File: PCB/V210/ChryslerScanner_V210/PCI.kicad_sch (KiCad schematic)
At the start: 15 parts, among them Q14 SI1555DL, U10 TS391C

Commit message: WIP
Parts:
- removed U10: TS391C, symbol ChryslerScanner:TS391C
- added U10: TS391RILT, Package_TO_SOT_SMD:SOT-23-5, symbol ChryslerScanner:TS391RILT
- C29, C30: footprint (none) -> Capacitor_SMD:C_0603_1608Metric
- D10: renamed from D18; value MSK4005 -> STPS0540Z; footprint (none) -> Britishideas:SOD-123; manf# (none) -> STPS0540Z
- D11: renamed from D19; value ESD585 -> ESD5B5; footprint (none) -> Diode_SMD:D_SOD-523; manf# (none) -> ESD5B5.0ST5G
- Q6: renamed from Q14; value SI1555DL -> BSD235CH6327XTSA1; footprint Package_TO_SOT_SMD:SOT-23-6 -> Package_TO_SOT_SMD:SOT-363_SC-70-6; manf# (none) -> BSD235CH6327XTSA1
- R36: renamed from R58; footprint (none) -> Resistor_SMD:R_0603_1608Metric
- R37: renamed from R59; footprint (none) -> Resistor_SMD:R_0603_1608Metric
- R38: renamed from R60; footprint (none) -> Resistor_SMD:R_0603_1608Metric
- R39: renamed from R61; footprint (none) -> Resistor_SMD:R_0603_1608Metric
- R40: renamed from R62; footprint (none) -> Resistor_SMD:R_0603_1608Metric
- R41: renamed from R63; footprint (none) -> Resistor_SMD:R_0603_1608Metric
- R42: renamed from R64; footprint (none) -> Resistor_SMD:R_0603_1608Metric
- R43: renamed from R65; footprint (none) -> Resistor_SMD:R_0603_1608Metric
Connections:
- net +12V: now also U10.5 (V+)
- net GND: now also U10.2 (V-)
- net PCI_RX: now also U10.1
- net at R38.1: now also U10.4 (+)
- net at R36.2, R37.1: now also U10.3 (-)
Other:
- title: Chrysler Scanner -> TJ Diag

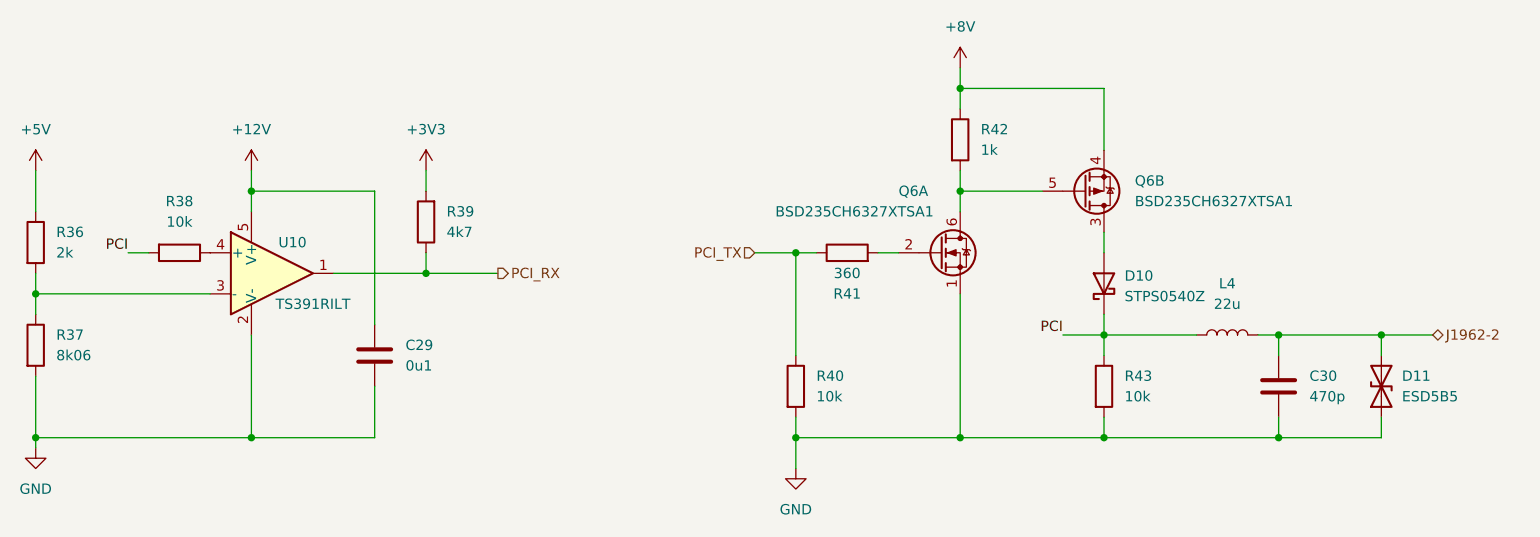
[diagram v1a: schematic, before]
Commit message: Added OBD-II connector.
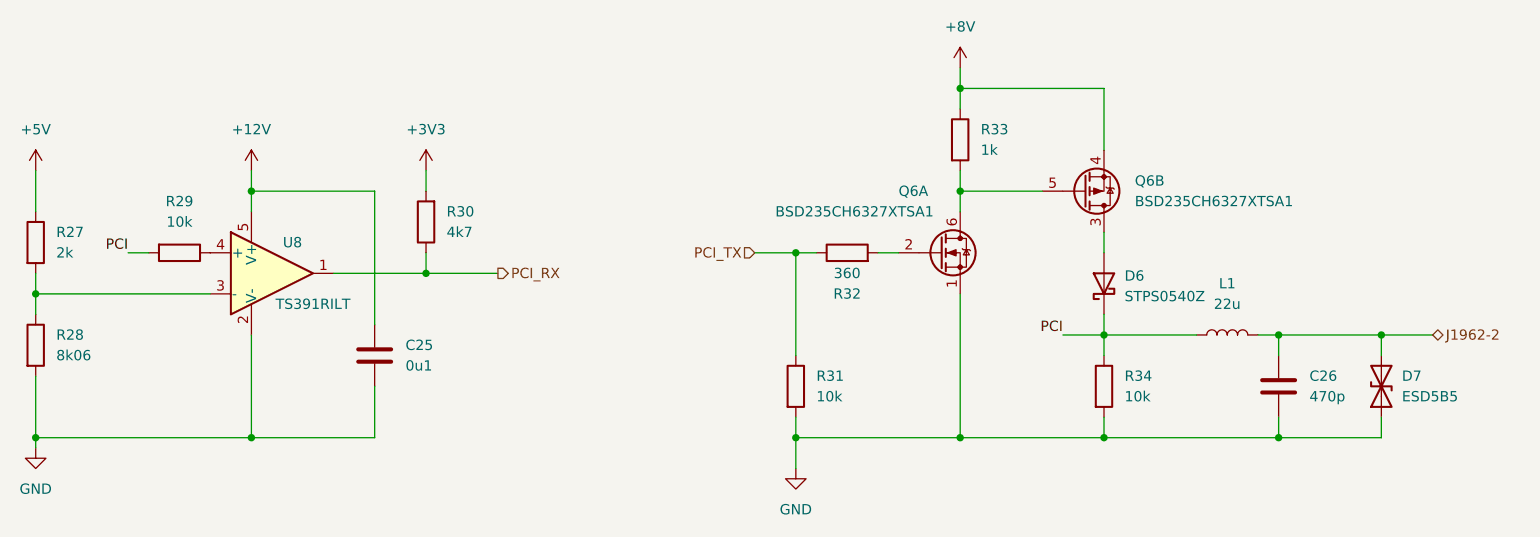
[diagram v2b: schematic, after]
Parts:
- renumbered C29 to C25, C30 to C26, D10 to D6, D11 to D7, L4 to L1, R36 to R27, R37 to R28, R38 to R29, R39 to R30, R40 to R31, R41 to R32, R42 to R33, R43 to R34, U10 to U8
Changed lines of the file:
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@@
   (title_block
     (title "TJ Diag")
-    (date "2023-07-01")
+    (date "2023-07-06")
     (rev "V1.00")
     (company "andy@britishideas.com")
     (comment 1 "V210/ChryslerScanner_V210/schematic/ChryslerScanner_V210_schematic.pdf")
-    (comment 2 "Developed From: https://github.com/laszlodaniel/ChryslerScanner/blob/master/PCB/")
+    (comment 2 "Based on: https://github.com/laszlodaniel/ChryslerScanner/blob/master/PCB/")
     (comment 3 "GPL V3 LICENSE")
   )
@@
   (symbol (lib_id "Device:R") (at 80.01 90.17 270) (unit 1)
     (in_bom yes) (on_board yes) (fields_autoplaced)
-    (property "Reference" "R38" (id 0) (at 80.01 83.82 90))
+    (property "Reference" "R29" (id 0) (at 80.01 83.82 90))
     (property "Value" "10k" (id 1) (at 80.01 86.36 90))
     (property "Footprint" "Resistor_SMD:R_0603_1608Metric" (id 2) (at 80.01 88.392 90)
@@
   (symbol (lib_id "power:+5V") (at 62.23 80.01 0) (unit 1)
     (in_bom yes) (on_board yes) (fields_autoplaced)
-    (property "Reference" "#PWR057" (id 0) (at 62.23 83.82 0)
+    (property "Reference" "#PWR047" (id 0) (at 62.23 83.82 0)
       (effects (font (size 1.27 1.27)) hide)
     )
@@
   (symbol (lib_id "ChryslerScanner:TS391RILT") (at 91.44 92.71 0) (unit 1)
     (in_bom yes) (on_board yes)
-    (property "Reference" "U10" (id 0) (at 93.98 88.9 0))
+    (property "Reference" "U8" (id 0) (at 93.98 88.9 0))
     (property "Value" "TS391RILT" (id 1) (at 96.52 96.52 0))
     (property "Footprint" "Package_TO_SOT_SMD:SOT-23-5" (id 2) (at 105.41 104.14 0)
@@
   (symbol (lib_id "Device:D_TVS") (at 228.6 106.68 90) (unit 1)
     (in_bom yes) (on_board yes) (fields_autoplaced)
-    (property "Reference" "D11" (id 0) (at 231.14 105.4099 90)
+    (property "Reference" "D7" (id 0) (at 231.14 105.4099 90)
       (effects (font (size 1.27 1.27)) (justify right))
     )
@@
   (symbol (lib_id "Device:R") (at 110.49 86.36 180) (unit 1)
     (in_bom yes) (on_board yes)
-    (property "Reference" "R39" (id 0) (at 113.03 85.0899 0)
+    (property "Reference" "R30" (id 0) (at 113.03 85.0899 0)
       (effects (font (size 1.27 1.27)) (justify right))
     )
@@
   (symbol (lib_id "Device:C") (at 104.14 102.87 0) (unit 1)
     (in_bom yes) (on_board yes) (fields_autoplaced)
-    (property "Reference" "C29" (id 0) (at 107.95 101.5999 0)
+    (property "Reference" "C25" (id 0) (at 107.95 101.5999 0)
       (effects (font (size 1.27 1.27)) (justify left))
     )
@@
   (symbol (lib_id "power:+8V") (at 176.53 67.31 0) (unit 1)
     (in_bom yes) (on_board yes) (fields_autoplaced)
-    (property "Reference" "#PWR062" (id 0) (at 176.53 71.12 0)
+    (property "Reference" "#PWR052" (id 0) (at 176.53 71.12 0)
       (effects (font (size 1.27 1.27)) hide)
     )
@@
   (symbol (lib_id "Device:R") (at 62.23 101.6 0) (unit 1)
     (in_bom yes) (on_board yes) (fields_autoplaced)
-    (property "Reference" "R37" (id 0) (at 64.77 100.3299 0)
+    (property "Reference" "R28" (id 0) (at 64.77 100.3299 0)
       (effects (font (size 1.27 1.27)) (justify left))
     )
@@
   (symbol (lib_id "Device:R") (at 156.21 106.68 0) (unit 1)
     (in_bom yes) (on_board yes) (fields_autoplaced)
-    (property "Reference" "R40" (id 0) (at 158.75 105.4099 0)
+    (property "Reference" "R31" (id 0) (at 158.75 105.4099 0)
       (effects (font (size 1.27 1.27)) (justify left))
     )
@@
   (symbol (lib_id "Device:R") (at 176.53 76.2 0) (unit 1)
     (in_bom yes) (on_board yes)
-    (property "Reference" "R42" (id 0) (at 179.07 74.9299 0)
+    (property "Reference" "R33" (id 0) (at 179.07 74.9299 0)
       (effects (font (size 1.27 1.27)) (justify left))
     )
@@
   (symbol (lib_id "Device:R") (at 62.23 88.9 0) (unit 1)
     (in_bom yes) (on_board yes) (fields_autoplaced)
-    (property "Reference" "R36" (id 0) (at 64.77 87.6299 0)
+    (property "Reference" "R27" (id 0) (at 64.77 87.6299 0)
       (effects (font (size 1.27 1.27)) (justify left))
     )
@@
   (symbol (lib_id "power:GND") (at 62.23 114.3 0) (unit 1)
     (in_bom yes) (on_board yes) (fields_autoplaced)
-    (property "Reference" "#PWR058" (id 0) (at 62.23 120.65 0)
+    (property "Reference" "#PWR048" (id 0) (at 62.23 120.65 0)
       (effects (font (size 1.27 1.27)) hide)
     )
@@
   (symbol (lib_id "Device:D_Schottky") (at 194.31 93.98 90) (unit 1)
     (in_bom yes) (on_board yes) (fields_autoplaced)
-    (property "Reference" "D10" (id 0) (at 196.85 93.0274 90)
+    (property "Reference" "D6" (id 0) (at 196.85 93.0274 90)
       (effects (font (size 1.27 1.27)) (justify right))
     )
@@
   (symbol (lib_id "Device:L") (at 209.55 100.33 90) (unit 1)
     (in_bom yes) (on_board yes) (fields_autoplaced)
-    (property "Reference" "L4" (id 0) (at 209.55 93.98 90))
+    (property "Reference" "L1" (id 0) (at 209.55 93.98 90))
     (property "Value" "22u" (id 1) (at 209.55 96.52 90))
     (property "Footprint" "" (id 2) (at 209.55 100.33 0)
@@
   (symbol (lib_id "Device:R") (at 194.31 106.68 0) (unit 1)
     (in_bom yes) (on_board yes) (fields_autoplaced)
-    (property "Reference" "R43" (id 0) (at 196.85 105.4099 0)
+    (property "Reference" "R34" (id 0) (at 196.85 105.4099 0)
       (effects (font (size 1.27 1.27)) (justify left))
     )
@@
   (symbol (lib_id "Device:C") (at 215.9 106.68 0) (unit 1)
     (in_bom yes) (on_board yes) (fields_autoplaced)
-    (property "Reference" "C30" (id 0) (at 219.71 105.4099 0)
+    (property "Reference" "C26" (id 0) (at 219.71 105.4099 0)
       (effects (font (size 1.27 1.27)) (justify left))
     )
@@
   (symbol (lib_id "Device:R") (at 162.56 90.17 90) (unit 1)
     (in_bom yes) (on_board yes)
-    (property "Reference" "R41" (id 0) (at 162.56 95.25 90))
+    (property "Reference" "R32" (id 0) (at 162.56 95.25 90))
     (property "Value" "360" (id 1) (at 162.56 92.71 90))
     (property "Footprint" "Resistor_SMD:R_0603_1608Metric" (id 2) (at 162.56 91.948 90)
@@
   (symbol (lib_id "power:GND") (at 156.21 116.84 0) (unit 1)
     (in_bom yes) (on_board yes) (fields_autoplaced)
-    (property "Reference" "#PWR061" (id 0) (at 156.21 123.19 0)
+    (property "Reference" "#PWR051" (id 0) (at 156.21 123.19 0)
       (effects (font (size 1.27 1.27)) hide)
     )
@@
   (symbol (lib_id "power:+12V") (at 88.9 80.01 0) (unit 1)
     (in_bom yes) (on_board yes) (fields_autoplaced)
-    (property "Reference" "#PWR059" (id 0) (at 88.9 83.82 0)
+    (property "Reference" "#PWR049" (id 0) (at 88.9 83.82 0)
       (effects (font (size 1.27 1.27)) hide)
     )
@@
   (symbol (lib_id "power:+3V3") (at 110.49 80.01 0) (unit 1)
     (in_bom yes) (on_board yes) (fields_autoplaced)
-    (property "Reference" "#PWR060" (id 0) (at 110.49 83.82 0)
-      (effects (font (size 1.27 1.27)) hide)
-    )
+    (property "Reference" "#PWR050" (id 0) (at 110.49 83.82 0)
+      (effects (font (size 1.27 1.27)) hide)
+    )

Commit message: Added CCD back in - needed for early TJs.
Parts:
- renumbered C25 to C23, C26 to C24, R27 to R25, R28 to R26, R29 to R27, R30 to R28, R31 to R29, R32 to R30, R33 to R31, R34 to R32
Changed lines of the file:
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@@
   (title_block
     (title "TJ Diag")
-    (date "2023-07-06")
+    (date "2023-07-07")
     (rev "V1.00")
     (company "andy@britishideas.com")
@@
   (symbol (lib_id "Device:R") (at 80.01 90.17 270) (unit 1)
     (in_bom yes) (on_board yes) (fields_autoplaced)
-    (property "Reference" "R29" (id 0) (at 80.01 83.82 90))
+    (property "Reference" "R27" (id 0) (at 80.01 83.82 90))
     (property "Value" "10k" (id 1) (at 80.01 86.36 90))
     (property "Footprint" "Resistor_SMD:R_0603_1608Metric" (id 2) (at 80.01 88.392 90)
@@
   (symbol (lib_id "power:+5V") (at 62.23 80.01 0) (unit 1)
     (in_bom yes) (on_board yes) (fields_autoplaced)
-    (property "Reference" "#PWR047" (id 0) (at 62.23 83.82 0)
+    (property "Reference" "#PWR043" (id 0) (at 62.23 83.82 0)
       (effects (font (size 1.27 1.27)) hide)
     )
@@
   (symbol (lib_id "Device:R") (at 110.49 86.36 180) (unit 1)
     (in_bom yes) (on_board yes)
-    (property "Reference" "R30" (id 0) (at 113.03 85.0899 0)
+    (property "Reference" "R28" (id 0) (at 113.03 85.0899 0)
       (effects (font (size 1.27 1.27)) (justify right))
     )
@@
   (symbol (lib_id "Device:C") (at 104.14 102.87 0) (unit 1)
     (in_bom yes) (on_board yes) (fields_autoplaced)
-    (property "Reference" "C25" (id 0) (at 107.95 101.5999 0)
+    (property "Reference" "C23" (id 0) (at 107.95 101.5999 0)
       (effects (font (size 1.27 1.27)) (justify left))
     )
@@
   (symbol (lib_id "power:+8V") (at 176.53 67.31 0) (unit 1)
     (in_bom yes) (on_board yes) (fields_autoplaced)
-    (property "Reference" "#PWR052" (id 0) (at 176.53 71.12 0)
+    (property "Reference" "#PWR048" (id 0) (at 176.53 71.12 0)
       (effects (font (size 1.27 1.27)) hide)
     )
@@
   (symbol (lib_id "Device:R") (at 62.23 101.6 0) (unit 1)
     (in_bom yes) (on_board yes) (fields_autoplaced)
-    (property "Reference" "R28" (id 0) (at 64.77 100.3299 0)
+    (property "Reference" "R26" (id 0) (at 64.77 100.3299 0)
       (effects (font (size 1.27 1.27)) (justify left))
     )
@@
   (symbol (lib_id "Device:R") (at 156.21 106.68 0) (unit 1)
     (in_bom yes) (on_board yes) (fields_autoplaced)
-    (property "Reference" "R31" (id 0) (at 158.75 105.4099 0)
+    (property "Reference" "R29" (id 0) (at 158.75 105.4099 0)
       (effects (font (size 1.27 1.27)) (justify left))
     )
@@
   (symbol (lib_id "Device:R") (at 176.53 76.2 0) (unit 1)
     (in_bom yes) (on_board yes)
-    (property "Reference" "R33" (id 0) (at 179.07 74.9299 0)
+    (property "Reference" "R31" (id 0) (at 179.07 74.9299 0)
       (effects (font (size 1.27 1.27)) (justify left))
     )
@@
   (symbol (lib_id "Device:R") (at 62.23 88.9 0) (unit 1)
     (in_bom yes) (on_board yes) (fields_autoplaced)
-    (property "Reference" "R27" (id 0) (at 64.77 87.6299 0)
+    (property "Reference" "R25" (id 0) (at 64.77 87.6299 0)
       (effects (font (size 1.27 1.27)) (justify left))
     )
@@
   (symbol (lib_id "power:GND") (at 62.23 114.3 0) (unit 1)
     (in_bom yes) (on_board yes) (fields_autoplaced)
-    (property "Reference" "#PWR048" (id 0) (at 62.23 120.65 0)
+    (property "Reference" "#PWR044" (id 0) (at 62.23 120.65 0)
       (effects (font (size 1.27 1.27)) hide)
     )
@@
   (symbol (lib_id "Device:R") (at 194.31 106.68 0) (unit 1)
     (in_bom yes) (on_board yes) (fields_autoplaced)
-    (property "Reference" "R34" (id 0) (at 196.85 105.4099 0)
+    (property "Reference" "R32" (id 0) (at 196.85 105.4099 0)
       (effects (font (size 1.27 1.27)) (justify left))
     )
@@
   (symbol (lib_id "Device:C") (at 215.9 106.68 0) (unit 1)
     (in_bom yes) (on_board yes) (fields_autoplaced)
-    (property "Reference" "C26" (id 0) (at 219.71 105.4099 0)
+    (property "Reference" "C24" (id 0) (at 219.71 105.4099 0)
       (effects (font (size 1.27 1.27)) (justify left))
     )
@@
   (symbol (lib_id "Device:R") (at 162.56 90.17 90) (unit 1)
     (in_bom yes) (on_board yes)
-    (property "Reference" "R32" (id 0) (at 162.56 95.25 90))
+    (property "Reference" "R30" (id 0) (at 162.56 95.25 90))
     (property "Value" "360" (id 1) (at 162.56 92.71 90))
     (property "Footprint" "Resistor_SMD:R_0603_1608Metric" (id 2) (at 162.56 91.948 90)
@@
   (symbol (lib_id "power:GND") (at 156.21 116.84 0) (unit 1)
     (in_bom yes) (on_board yes) (fields_autoplaced)
-    (property "Reference" "#PWR051" (id 0) (at 156.21 123.19 0)
+    (property "Reference" "#PWR047" (id 0) (at 156.21 123.19 0)
       (effects (font (size 1.27 1.27)) hide)
     )
@@
   (symbol (lib_id "power:+12V") (at 88.9 80.01 0) (unit 1)
     (in_bom yes) (on_board yes) (fields_autoplaced)
-    (property "Reference" "#PWR049" (id 0) (at 88.9 83.82 0)
+    (property "Reference" "#PWR045" (id 0) (at 88.9 83.82 0)
       (effects (font (size 1.27 1.27)) hide)
     )
@@
   (symbol (lib_id "power:+3V3") (at 110.49 80.01 0) (unit 1)
     (in_bom yes) (on_board yes) (fields_autoplaced)
-    (property "Reference" "#PWR050" (id 0) (at 110.49 83.82 0)
-      (effects (font (size 1.27 1.27)) hide)
-    )
+    (property "Reference" "#PWR046" (id 0) (at 110.49 83.82 0)
+      (effects (font (size 1.27 1.27)) hide)
+    )

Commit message: Final component assignments.
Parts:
- L1: footprint (none) -> Inductor_SMD:L_0805_2012Metric; manf# (none) -> MLZ2012P220WT000
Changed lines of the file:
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@@
   (title_block
     (title "TJ Diag")
-    (date "2023-07-07")
+    (date "2023-07-18")
     (rev "V1.00")
     (company "andy@britishideas.com")
@@
     (property "Reference" "L1" (id 0) (at 209.55 93.98 90))
     (property "Value" "22u" (id 1) (at 209.55 96.52 90))
-    (property "Footprint" "" (id 2) (at 209.55 100.33 0)
+    (property "Footprint" "Inductor_SMD:L_0805_2012Metric" (id 2) (at 209.55 100.33 0)
       (effects (font (size 1.27 1.27)) hide)
     )
@@
       (effects (font (size 1.27 1.27)) hide)
     )
+    (property "manf#" "MLZ2012P220WT000" (id 4) (at 209.55 100.33 90)
+      (effects (font (size 1.27 1.27)) hide)
+    )
